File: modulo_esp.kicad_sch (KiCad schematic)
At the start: 3 parts

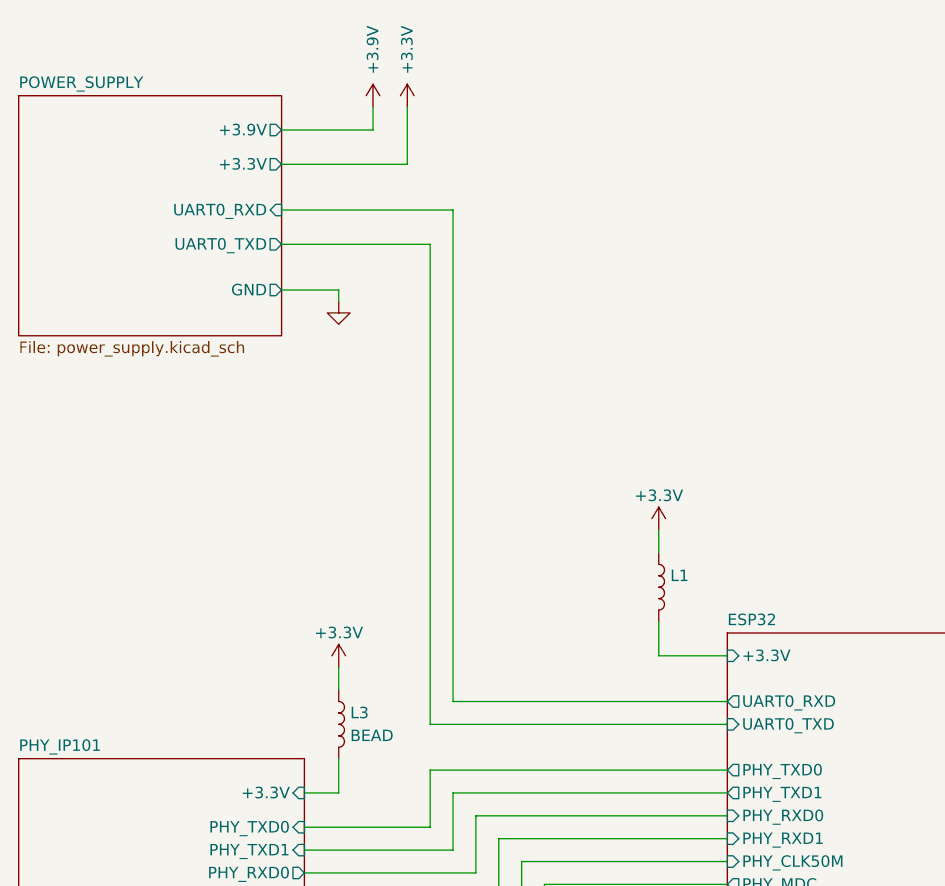
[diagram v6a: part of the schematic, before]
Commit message: Adicionado duas barras de pinos 1x10
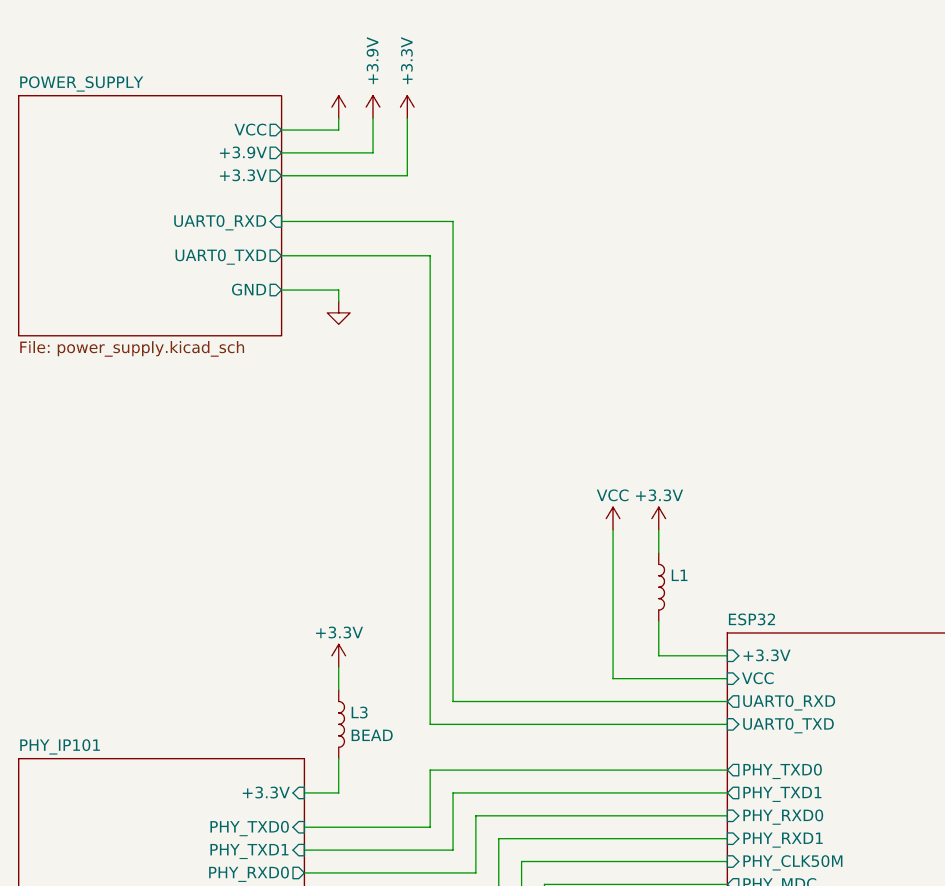
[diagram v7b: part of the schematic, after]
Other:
- sheet ESP32 ports: added VCC; removed none
- sheet POWER_SUPPLY ports: added VCC; removed none
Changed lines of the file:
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@@
     (comment 2 "Variant 1: Full")
   )
+  (wire (pts (xy 73.66 34.29) (xy 80.01 34.29))
+    (stroke (width 0) (type default) (color 0 0 0 0))
+  )
   (wire (pts (xy 185.42 97.79) (xy 185.42 115.57))
     (stroke (width 0) (type default) (color 0 0 0 0))
@@
     (stroke (width 0) (type default) (color 0 0 0 0))
   )
-  (wire (pts (xy 87.63 31.75) (xy 87.63 38.1))
+  (wire (pts (xy 87.63 33.02) (xy 87.63 39.37))
     (stroke (width 0) (type default) (color 0 0 0 0))
   )
@@
     (stroke (width 0) (type default) (color 0 0 0 0))
   )
+  (wire (pts (xy 110.49 78.74) (xy 110.49 95.25))
+    (stroke (width 0) (type default) (color 0 0 0 0))
+  )
   (wire (pts (xy 76.2 124.46) (xy 102.87 124.46))
     (stroke (width 0) (type default) (color 0 0 0 0))
@@
     (stroke (width 0) (type default) (color 0 0 0 0))
   )
-  (wire (pts (xy 90.17 46.99) (xy 90.17 100.33))
+  (wire (pts (xy 90.17 48.26) (xy 90.17 100.33))
     (stroke (width 0) (type default) (color 0 0 0 0))
   )
@@
     (stroke (width 0) (type default) (color 0 0 0 0))
   )
-  (wire (pts (xy 92.71 43.18) (xy 92.71 97.79))
-    (stroke (width 0) (type default) (color 0 0 0 0))
-  )
-  (wire (pts (xy 83.82 34.29) (xy 73.66 34.29))
+  (wire (pts (xy 92.71 44.45) (xy 92.71 97.79))
+    (stroke (width 0) (type default) (color 0 0 0 0))
+  )
+  (wire (pts (xy 73.66 36.83) (xy 83.82 36.83))
     (stroke (width 0) (type default) (color 0 0 0 0))
   )
@@
     (stroke (width 0) (type default) (color 0 0 0 0))
   )
+  (wire (pts (xy 110.49 95.25) (xy 123.19 95.25))
+    (stroke (width 0) (type default) (color 0 0 0 0))
+  )
   (wire (pts (xy 100.33 115.57) (xy 123.19 115.57))
     (stroke (width 0) (type default) (color 0 0 0 0))
@@
     (stroke (width 0) (type default) (color 0 0 0 0))
   )
-  (wire (pts (xy 73.66 46.99) (xy 90.17 46.99))
+  (wire (pts (xy 73.66 48.26) (xy 90.17 48.26))
     (stroke (width 0) (type default) (color 0 0 0 0))
   )
@@
     (stroke (width 0) (type default) (color 0 0 0 0))
   )
-  (wire (pts (xy 83.82 31.75) (xy 83.82 34.29))
+  (wire (pts (xy 80.01 34.29) (xy 80.01 33.02))
+    (stroke (width 0) (type default) (color 0 0 0 0))
+  )
+  (wire (pts (xy 83.82 33.02) (xy 83.82 36.83))
     (stroke (width 0) (type default) (color 0 0 0 0))
   )
@@
     (stroke (width 0) (type default) (color 0 0 0 0))
   )
-  (wire (pts (xy 73.66 43.18) (xy 92.71 43.18))
+  (wire (pts (xy 73.66 44.45) (xy 92.71 44.45))
     (stroke (width 0) (type default) (color 0 0 0 0))
   )
@@
     (stroke (width 0) (type default) (color 0 0 0 0))
   )
-  (wire (pts (xy 87.63 38.1) (xy 73.66 38.1))
+  (wire (pts (xy 87.63 39.37) (xy 73.66 39.37))
     (stroke (width 0) (type default) (color 0 0 0 0))
   )
@@
     (stroke (width 0) (type default) (color 0 0 0 0))
   )
-  (symbol (lib_id "Alexandre_Library:Power") (at 83.82 31.75 0) (unit 1)
+  (symbol (lib_id "Alexandre_Library:Power") (at 83.82 33.02 0) (unit 1)
     (in_bom yes) (on_board yes)
-    (property "Reference" "#PWR1" (id 0) (at 83.82 24.13 0)
-      (effects (font (size 1.27 1.27)) hide)
-    )
-    (property "Value" "+3.9V" (id 1) (at 83.82 25.4 90))
-    (property "Footprint" "" (id 2) (at 83.82 31.75 0)
-      (effects (font (size 1.27 1.27)) hide)
-    )
-    (property "Datasheet" "" (id 3) (at 83.82 31.75 0)
+    (property "Reference" "#PWR1" (id 0) (at 83.82 25.4 0)
+      (effects (font (size 1.27 1.27)) hide)
+    )
+    (property "Value" "+3.9V" (id 1) (at 83.82 26.67 90))
+    (property "Footprint" "" (id 2) (at 83.82 33.02 0)
+      (effects (font (size 1.27 1.27)) hide)
+    )
+    (property "Datasheet" "" (id 3) (at 83.82 33.02 0)
       (effects (font (size 1.27 1.27)) hide)
     )
@@
     (pin "1")
   )
+  (symbol (lib_id "Alexandre_Library:Power") (at 110.49 78.74 0) (unit 1)
+    (in_bom yes) (on_board yes)
+    (property "Reference" "#PWR?" (id 0) (at 110.49 71.12 0)
+      (effects (font (size 1.27 1.27)) hide)
+    )
+    (property "Value" "VCC" (id 1) (at 110.49 74.93 0))
+    (property "Footprint" "" (id 2) (at 110.49 78.74 0)
+      (effects (font (size 1.27 1.27)) hide)
+    )
+    (property "Datasheet" "" (id 3) (at 110.49 78.74 0)
+      (effects (font (size 1.27 1.27)) hide)
+    )
+    (pin "1")
+  )
   (symbol (lib_id "power:GND") (at 120.65 133.35 0) (unit 1)
     (in_bom yes) (on_board yes) (fields_autoplaced)
@@
     (pin "1")
   )
-  (symbol (lib_id "power:+3.3V") (at 87.63 31.75 0) (unit 1)
+  (symbol (lib_id "power:+3.3V") (at 87.63 33.02 0) (unit 1)
     (in_bom yes) (on_board yes)
-    (property "Reference" "#PWR02" (id 0) (at 87.63 35.56 0)
-      (effects (font (size 1.27 1.27)) hide)
-    )
-    (property "Value" "+3.3V" (id 1) (at 87.63 25.4 90))
-    (property "Footprint" "" (id 2) (at 87.63 31.75 0)
-      (effects (font (size 1.27 1.27)) hide)
-    )
-    (property "Datasheet" "" (id 3) (at 87.63 31.75 0)
+    (property "Reference" "#PWR02" (id 0) (at 87.63 36.83 0)
+      (effects (font (size 1.27 1.27)) hide)
+    )
+    (property "Value" "+3.3V" (id 1) (at 87.63 26.67 90))
+    (property "Footprint" "" (id 2) (at 87.63 33.02 0)
+      (effects (font (size 1.27 1.27)) hide)
+    )
+    (property "Datasheet" "" (id 3) (at 87.63 33.02 0)
       (effects (font (size 1.27 1.27)) hide)
     )
@@
     )
     (property "Datasheet" "" (id 3) (at 209.55 130.81 0)
+      (effects (font (size 1.27 1.27)) hide)
+    )
+    (pin "1")
+  )
+  (symbol (lib_id "Alexandre_Library:Power") (at 80.01 33.02 0) (unit 1)
+    (in_bom yes) (on_board yes)
+    (property "Reference" "#PWR?" (id 0) (at 80.01 25.4 0)
+      (effects (font (size 1.27 1.27)) hide)
+    )
+    (property "Value" "" (id 1) (at 80.01 27.94 90))
+    (property "Footprint" "" (id 2) (at 80.01 33.02 0)
+      (effects (font (size 1.27 1.27)) hide)
+    )
+    (property "Datasheet" "" (id 3) (at 80.01 33.02 0)
       (effects (font (size 1.27 1.27)) hide)
     )
@@
       (effects (font (size 1.27 1.27)) (justify left top))
     )
-    (pin "+3.9V" output (at 73.66 34.29 0)
-      (effects (font (size 1.27 1.27)) (justify right))
-    )
-    (pin "+3.3V" output (at 73.66 38.1 0)
-      (effects (font (size 1.27 1.27)) (justify right))
-    )
-    (pin "UART0_RXD" input (at 73.66 43.18 0)
-      (effects (font (size 1.27 1.27)) (justify right))
-    )
-    (pin "UART0_TXD" output (at 73.66 46.99 0)
+    (pin "+3.9V" output (at 73.66 36.83 0)
+      (effects (font (size 1.27 1.27)) (justify right))
+    )
+    (pin "+3.3V" output (at 73.66 39.37 0)
+      (effects (font (size 1.27 1.27)) (justify right))
+    )
+    (pin "UART0_RXD" input (at 73.66 44.45 0)
+      (effects (font (size 1.27 1.27)) (justify right))
+    )
+    (pin "UART0_TXD" output (at 73.66 48.26 0)
       (effects (font (size 1.27 1.27)) (justify right))
     )
     (pin "GND" output (at 73.66 52.07 0)
+      (effects (font (size 1.27 1.27)) (justify right))
+    )
+    (pin "VCC" output (at 73.66 34.29 0)
       (effects (font (size 1.27 1.27)) (justify right))
     )
@@
     (pin "BG95_PWRKEY" output (at 165.1 107.95 0)
       (effects (font (size 1.27 1.27)) (justify right))
+    )
+    (pin "VCC" input (at 123.19 95.25 180)
+      (effects (font (size 1.27 1.27)) (justify left))
     )
   )
@@
       (reference "#PWR069") (unit 1) (value "+3.3V") (footprint "")
     )
-    (path "/fad468d2-9036-4024-8b69-088056b4a2a2/d479ba82-6df0-4344-aa5e-f453673c07e7"
-      (reference "#PWR070") (unit 1) (value "+3.3V") (footprint "")
-    )
     (path "/fad468d2-9036-4024-8b69-088056b4a2a2/5c3e39fe-b953-440e-afb3-f8bf1d0b3bb4"
       (reference "#PWR071") (unit 1) (value "+3.3V") (footprint "")
@@
       (reference "#PWR126") (unit 1) (value "+3.9V") (footprint "")
     )
+    (path "/563459a3-a7fd-4b2e-9a99-1de4a36b5fc0"
+      (reference "#PWR?") (unit 1) (value "VCC") (footprint "")
+    )
+    (path "/f2c6cb8d-5d0b-4a49-9d75-60e62e54e83b"
+      (reference "#PWR?") (unit 1) (value "VCC") (footprint "")
+    )
     (path "/32e232d5-57bb-46e3-a8e5-df7ec6f170f8/fbcd98bd-9c30-4cee-b873-daa3b82f675c"

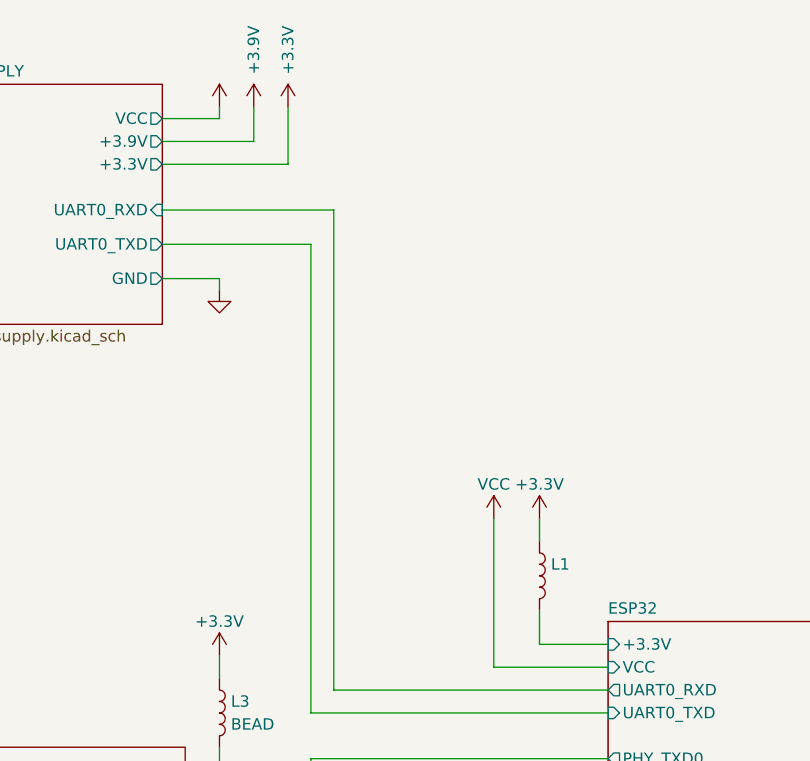
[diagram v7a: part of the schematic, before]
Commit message: Atualização das referências dos componentes
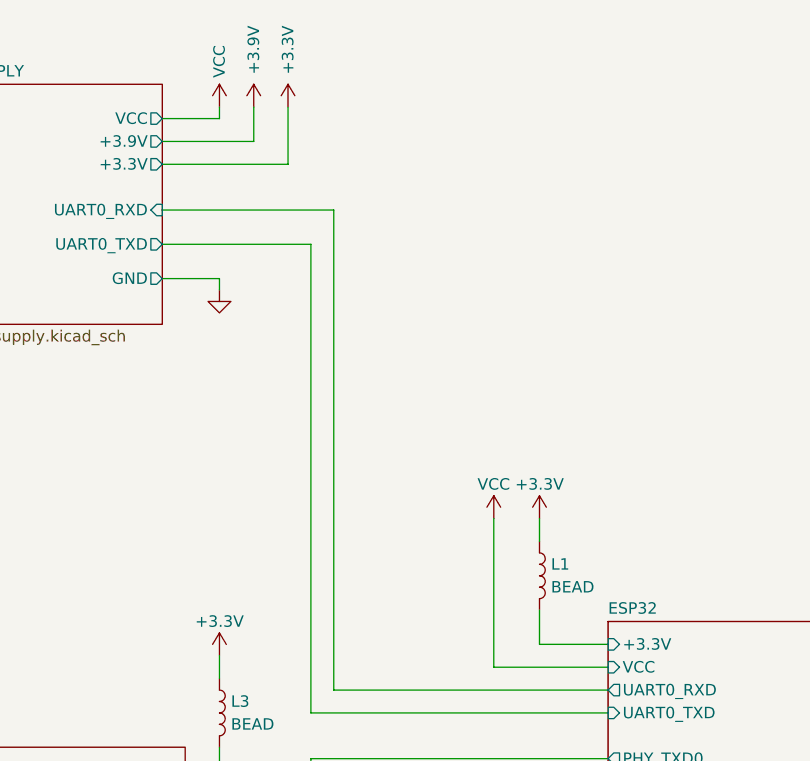
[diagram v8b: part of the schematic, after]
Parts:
- L1: value (none) -> BEAD; footprint (none) -> Inductor_SMD:L_0603_1608Metric_Pad1.05x0.95mm_HandSolder
